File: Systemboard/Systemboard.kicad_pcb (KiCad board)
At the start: 2 copper layers, 175 x 135 mm, 206 parts, among them J1 Conn_01x60, J108 Prog BT, J2 Conn_01x02, J3 Conn_01x01, J4 Conn_01x01, Q1 MMBT5551L, Q2 MMBT5551L, Q3 MMBT5551L, Q4 MMBT5551L, Q5 MMBT5551L, U1 INA226, U10 74HC595, U101 ESP32-WROOM-32E, U103 TLV73333PDBV, U104 PCM2706CPJTR, U11 74HC14, U2 LM358, U201 TLV73333PDBV, U202 PCM5102A, U3 J104D2C12VDC.15S, U301 TLV73333PDBV, U4 J104D2C12VDC.15S, U5 LM2596S-5, U501 TPA3118D2DAPR, U6 LM2596S-3.3, U7 LM2596S-5, U8 LM2596S-ADJ, U9 LTV-817S, Y101 CSTNE12M0G55A000R0

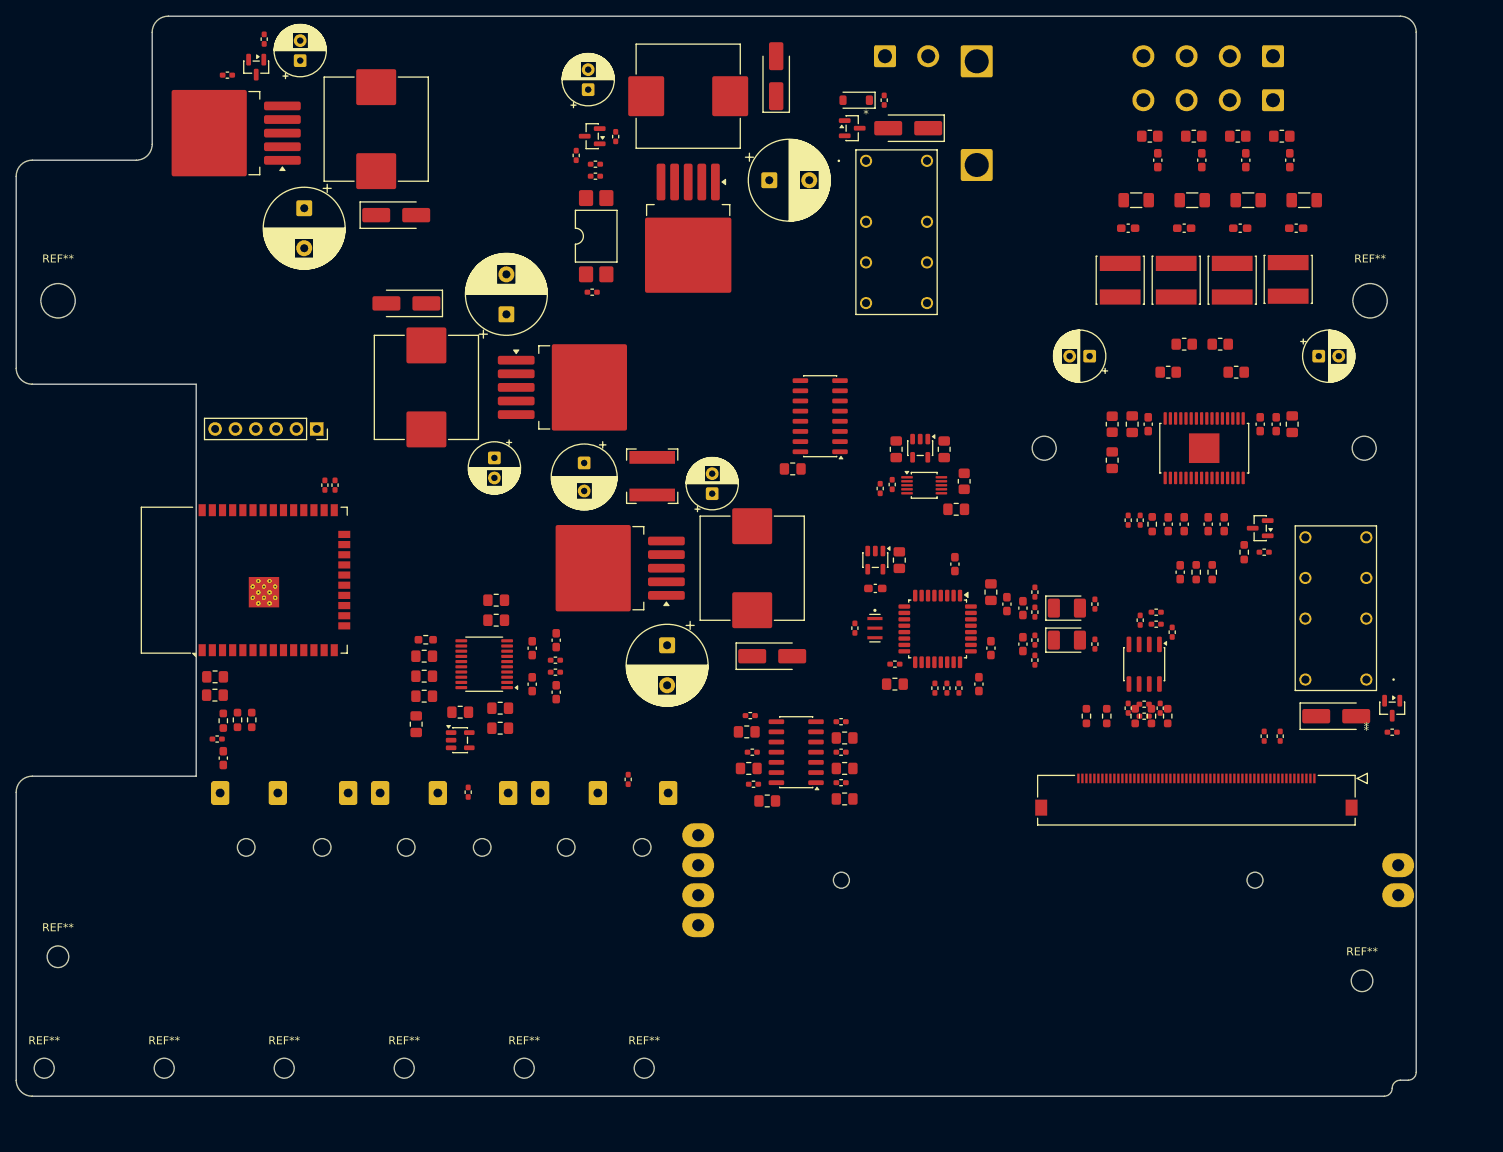
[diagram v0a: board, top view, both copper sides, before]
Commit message: move pot closer to edge
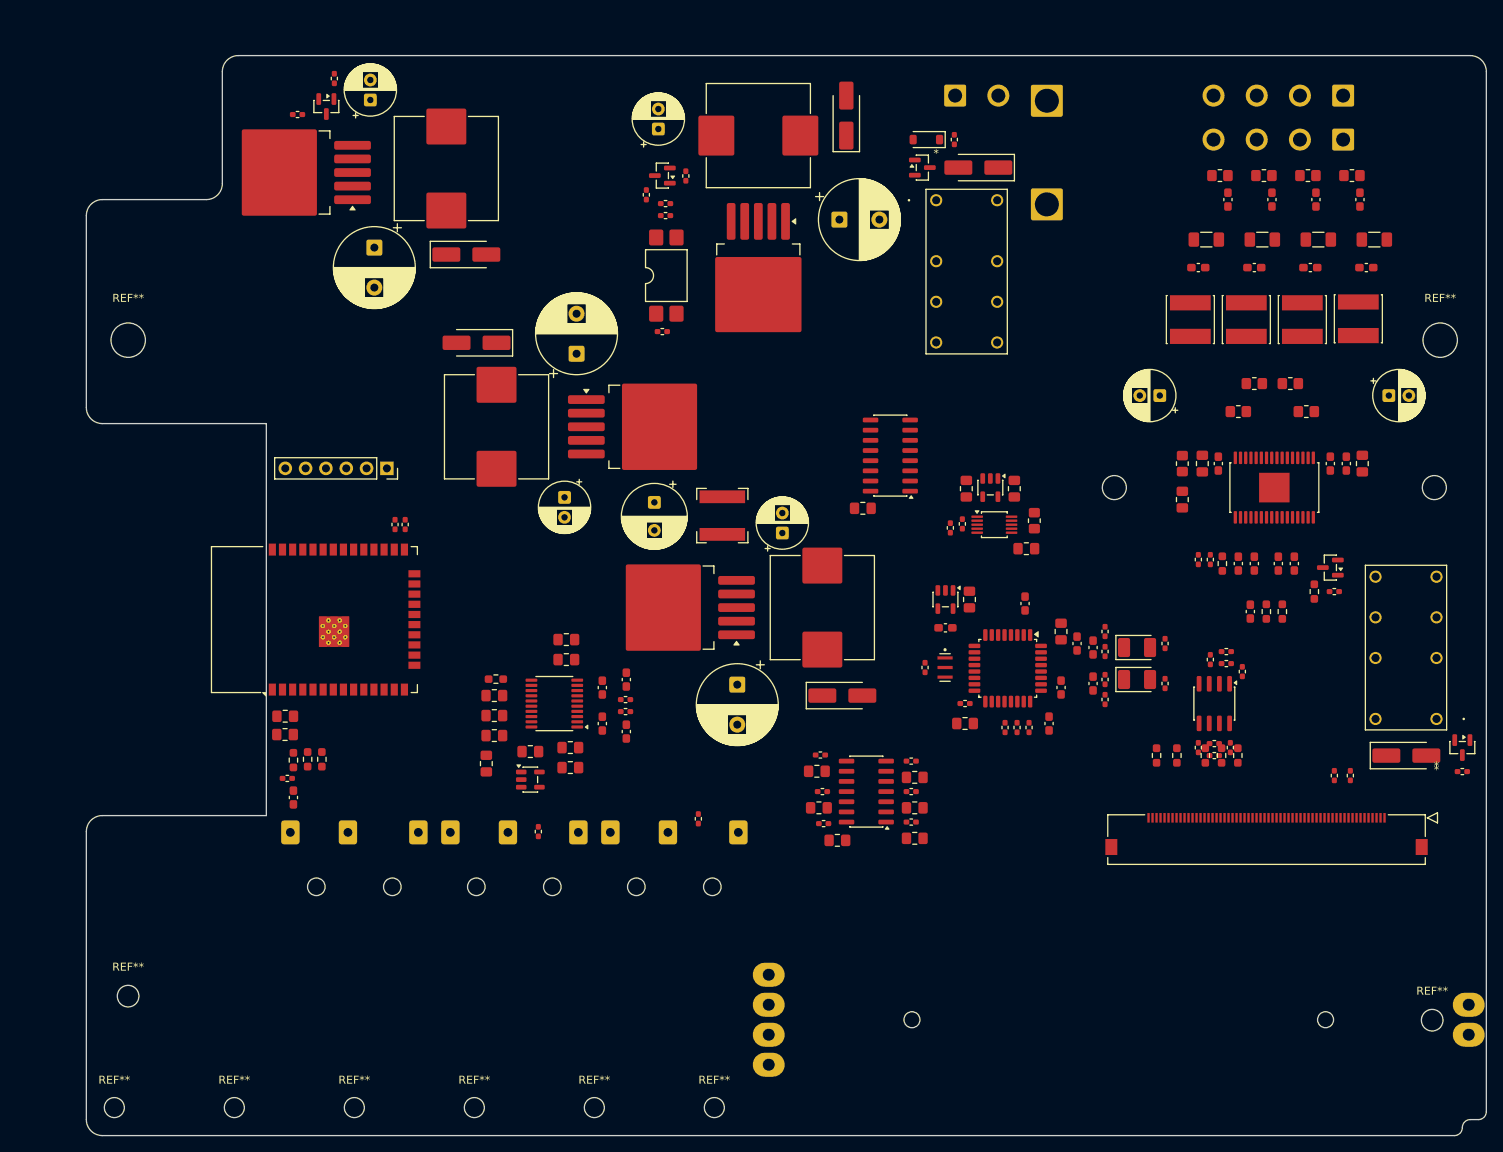
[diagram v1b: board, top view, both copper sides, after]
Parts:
- moved RV1 19.5 mm to (180.8, 144.9)
- moved C106 10.1 mm to (143.3, 118.5)
- moved C35 10.1 mm to (185.9, 66.9)
- moved R102 10.1 mm to (185.5, 111.9)
- moved R109 10.1 mm to (143.5, 111.9)
- moved R112 10.1 mm to (195.7, 111.9)
- moved R113 10.1 mm to (143.9, 120.4)
- moved U3 10.1 mm to (220.5, 107.3)
- moved C14 10.1 mm to (211.0, 42.4)
- moved C15 10.1 mm to (200.0, 42.4)
- moved C16 10.1 mm to (205.5, 42.4)
- moved C17 10.1 mm to (194.5, 42.4)
- moved J2 10.1 mm to (160.4, 29.4)
- moved R3 10.1 mm to (210.0, 39.4)
- moved R4 10.1 mm to (199.0, 39.4)
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
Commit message: prepare for autoroute
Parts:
- moved R114 4.12 mm to (191.0, 96.0)
- moved R116 4.12 mm to (189.5, 107.0)
- moved R128 4.12 mm to (193.0, 95.0)
- moved R129 4.12 mm to (193.0, 96.5)
- moved R130 4.12 mm to (191.5, 106.5)
- moved R131 4.12 mm to (191.5, 108.0)
- moved R132 4.12 mm to (195.0, 97.5)
- moved R133 4.12 mm to (193.5, 107.0)
- moved U2 4.12 mm to (191.5, 101.5)
- moved C201 2.76 mm to (99.5, 114.5)
- moved C202 2.76 mm to (105.0, 113.0)
- moved C203 2.76 mm to (114.0, 105.0)
- moved C204 2.76 mm to (117.0, 110.5)
- moved C205 2.76 mm to (110.0, 112.5)
- moved C206 2.76 mm to (100.5, 108.5)
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- renumbered REF** to H1, REF** to H10, REF** to H11, REF** to H13, REF** to H14, REF** to H2, REF** to H4, REF** to H5, REF** to H6, REF** to H7, REF** to H8, REF** to H9, REF** to SW_Dummy
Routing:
- net /DAC_D+: track 0.00 -> 51.1 mm
- net /DAC_D-: track 0.00 -> 50.4 mm
- net +12V: track 0.00 -> 37.7 mm
- net /Speaker_PR: track 0.00 -> 27.1 mm
- net /Speaker_NL: track 0.00 -> 26.9 mm
- net /Speaker_NR: track 0.00 -> 26.4 mm
- net /Speaker_PL: track 0.00 -> 26.4 mm
- net Net-(U7-FB): track 0.00 -> 25.4 mm
- net GND: track 0.00 -> 24.7 mm, vias 0 -> 12
- net +5V: track 0.00 -> 21.8 mm
- net +3V3: track 0.00 -> 20.9 mm
- net Net-(U501-OUTNL): track 0.00 -> 18.7 mm
- net Net-(D1-K): track 0.00 -> 18.5 mm
- net Net-(U501-OUTPR): track 0.00 -> 18.3 mm
- net Net-(D3-K): track 0.00 -> 17.9 mm
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- added copper zone on F.Cu, net +12V
- added copper zone on F.Cu, net GND

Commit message: differential
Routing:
- net /DAC_D-: track 50.4 -> 68.0 mm
- net /DAC_D+: track 51.1 -> 66.5 mm
- net GND: vias 12 -> 74
